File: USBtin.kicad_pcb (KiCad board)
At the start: 2 copper layers, 65 x 32 mm, 21 parts, among them IC1 MCP2515-I_P, J1 USB_B, J2 Conn_01x03, U1 PIC18F14K50-EP, U2 MCP2551-I-P, Y1 24MHz

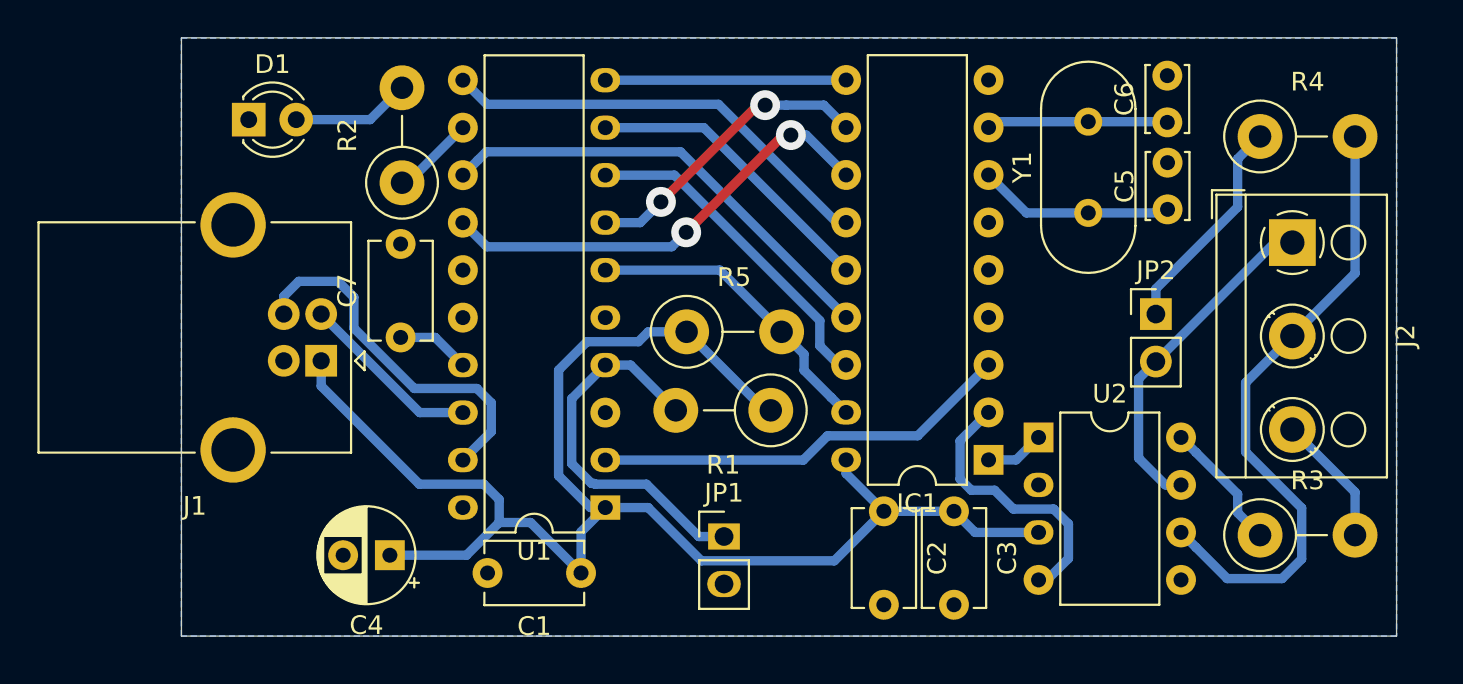
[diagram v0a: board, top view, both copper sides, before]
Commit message: changing C4 to a polarize capacitor
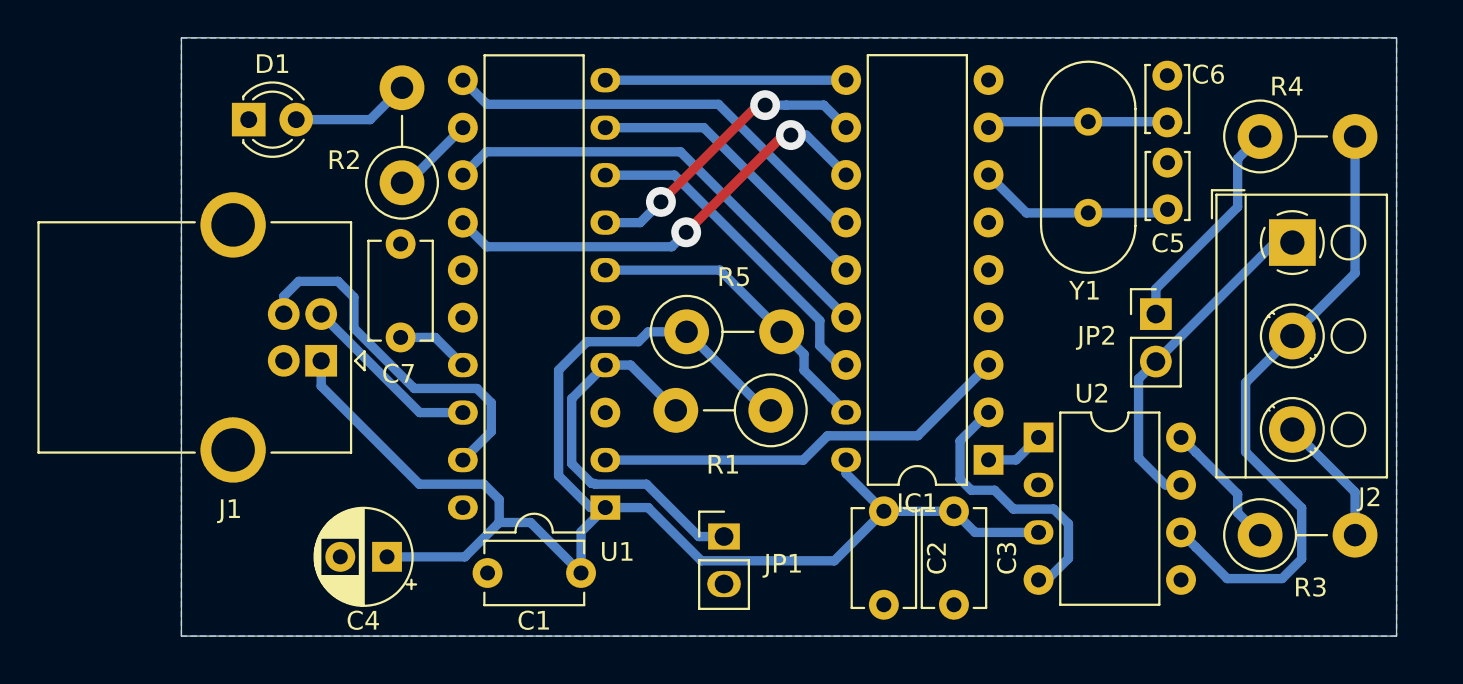
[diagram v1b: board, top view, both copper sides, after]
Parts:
- moved C4 0.18 mm to (111.0, 127.8)
